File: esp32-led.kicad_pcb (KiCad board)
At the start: 2 copper layers, 50.8 x 56.2 mm, 14 parts, among them J1 LED Connector, J2 USB4125-GF-A_REVA2, J3 LED Connector, U1 SN74AHCT125D, U2 ESP32_NODEMCU

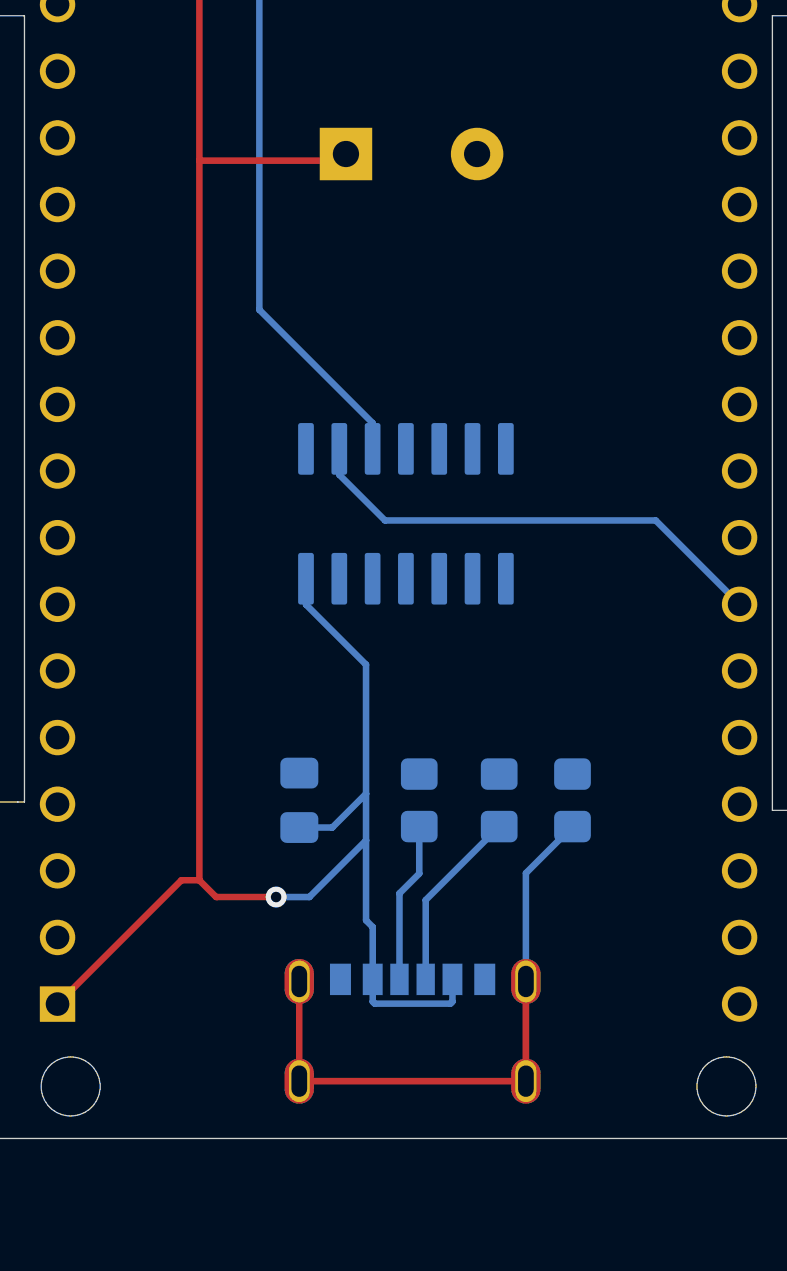
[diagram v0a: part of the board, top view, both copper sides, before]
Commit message: Added barrel jack version
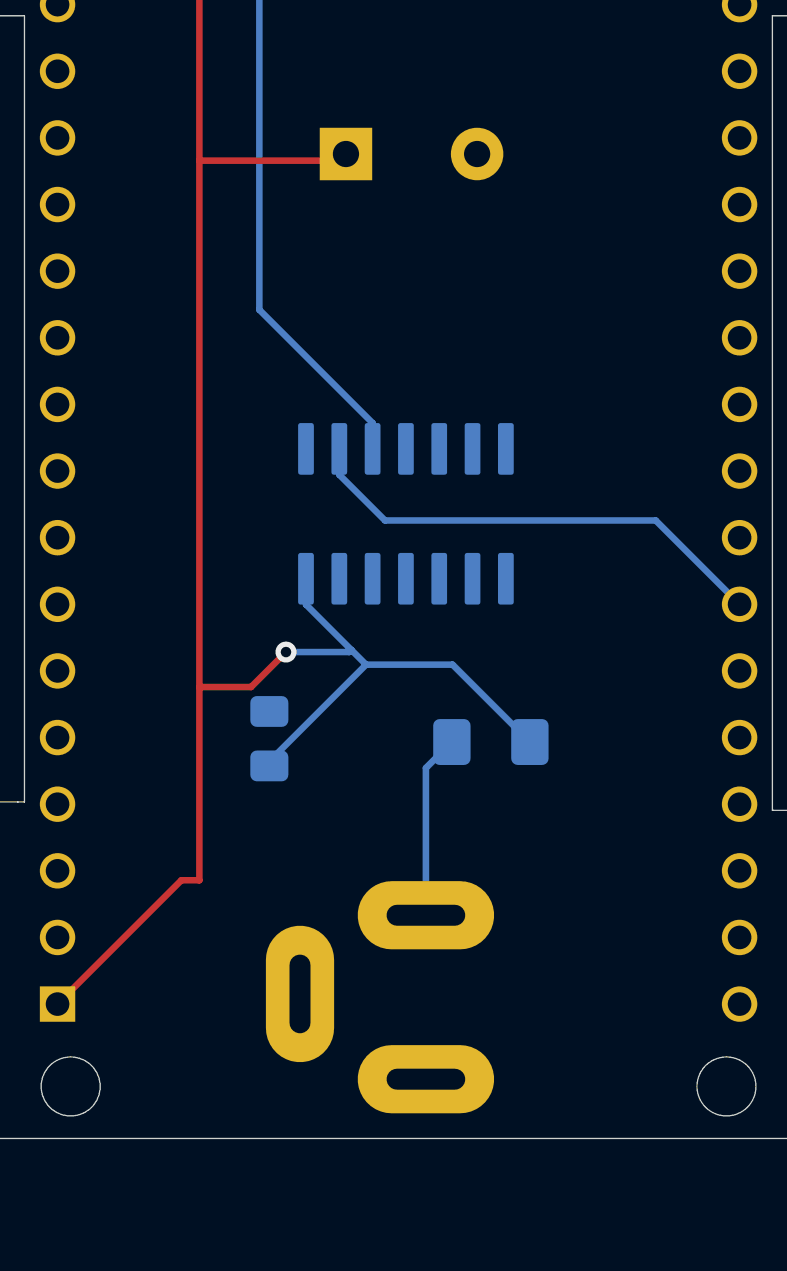
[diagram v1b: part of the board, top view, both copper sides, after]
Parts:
- removed R1, R2: 5.11K, Resistor_SMD:R_0805_2012Metric_Pad1.20x1.40mm_HandSolder
- removed R3: 1M, Resistor_SMD:R_0805_2012Metric_Pad1.20x1.40mm_HandSolder
- added F1: Fuse max 6A, Fuse:Fuse_1206_3216Metric_Pad1.42x1.75mm_HandSolder, B.Cu at (170.6, 86.2)
- J2: value USB4125-GF-A_REVA2 -> 54-00167; footprint USB4125-GF-A_REVA2:GCT_USB4125-GF-A_REVA2 -> 54-00167:TENSILITY_54-00167
- moved J2 8.24 mm to (168.1, 106.5), turned to 90 degrees
- moved C2 2.61 mm to (162.2, 86.0)
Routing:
- net Net-(J2-PadS1): track 22.9 -> 0.00 mm
- net +5V: track 104.7 -> 96.4 mm
- net Net-(F1-Pad1): track 0.00 -> 7.01 mm
- net Net-(J2-PadA5): track 6.99 -> 0.00 mm
- net Net-(J2-PadB5): track 6.14 -> 0.00 mm

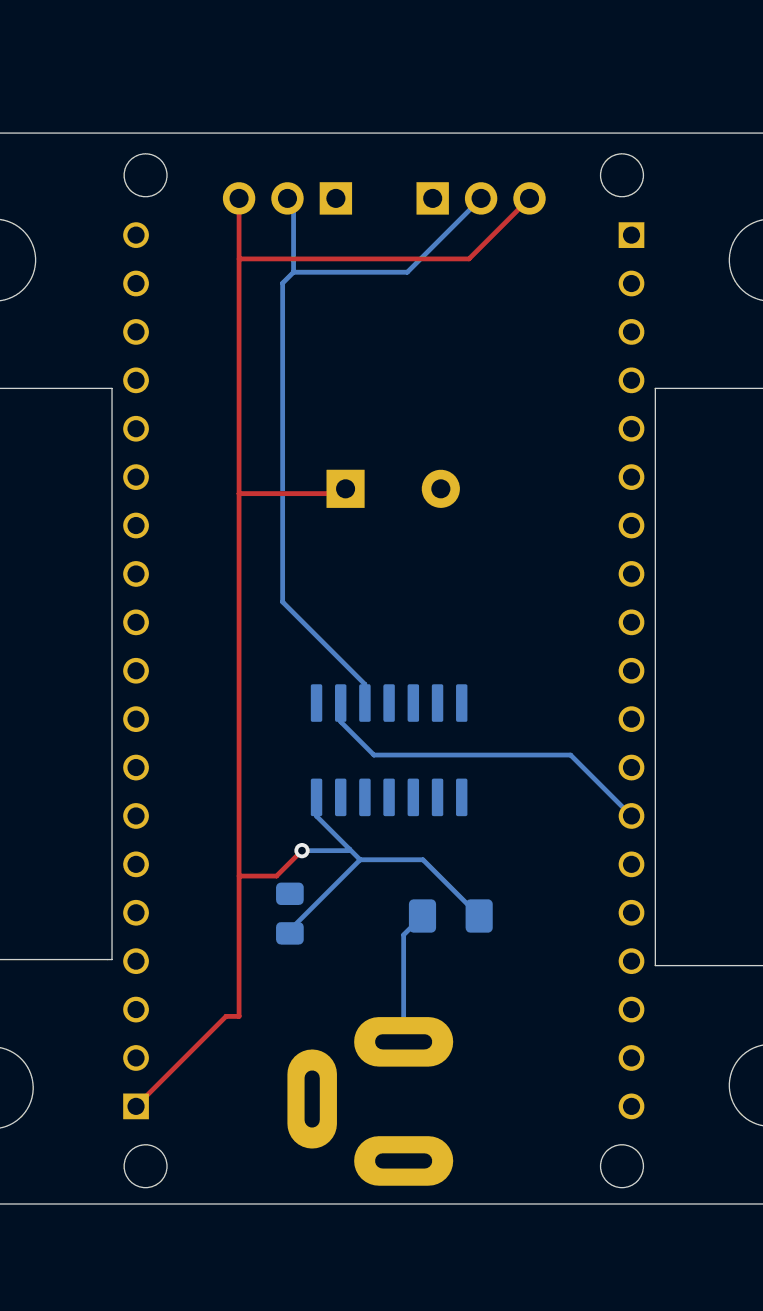
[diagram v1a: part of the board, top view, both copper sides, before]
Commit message: Changed the wrong esp32 footprint
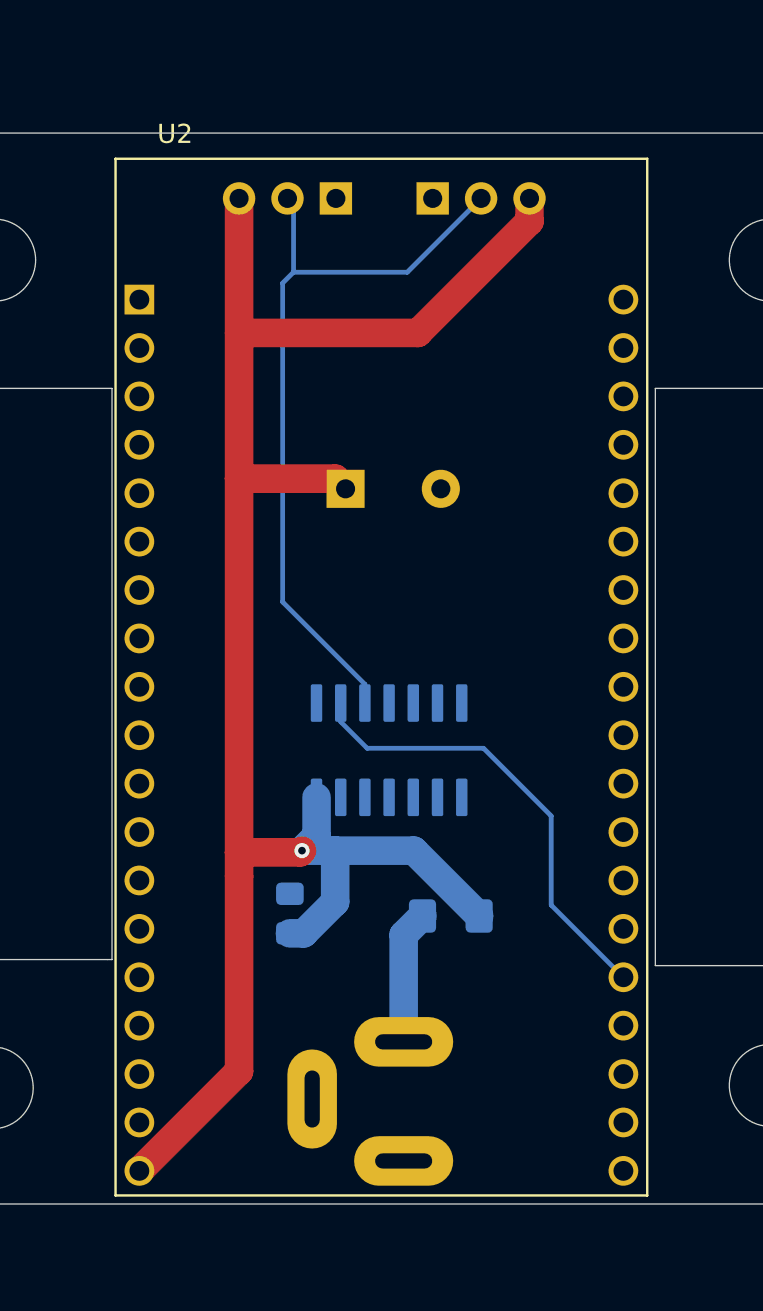
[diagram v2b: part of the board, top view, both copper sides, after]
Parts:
- U2: value ESP32_NODEMCU -> ESP32-DEVKITC-32D; footprint ESP32_NODEMCU:MODULE_ESP32_NODEMCU -> ESP32-DEVKITC-32D:MODULE_ESP32-DEVKITC-32D
- moved U2 0.31 mm to (167.0, 73.6)
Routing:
- net +5V: track 96.4 -> 102.8 mm
- net GPIO4: track 18.3 -> 24.1 mm
